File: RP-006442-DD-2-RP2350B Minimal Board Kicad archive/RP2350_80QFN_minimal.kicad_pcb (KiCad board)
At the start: 2 copper layers, 52 x 71.5 mm, 49 parts, among them J1 USB_B_Micro, J2 Conn_02x26_Odd_Even, J3 Conn_02x26_Odd_Even, J4 SM03B-SRSS-TB, SW1 SW_Push, SW2 SW_Push, U1 RP2350_80QFN, U2 NCP1117-3.3_SOT223, U3 W25Q128JVS, U4 DNF, Y1 ABM8-272-T3

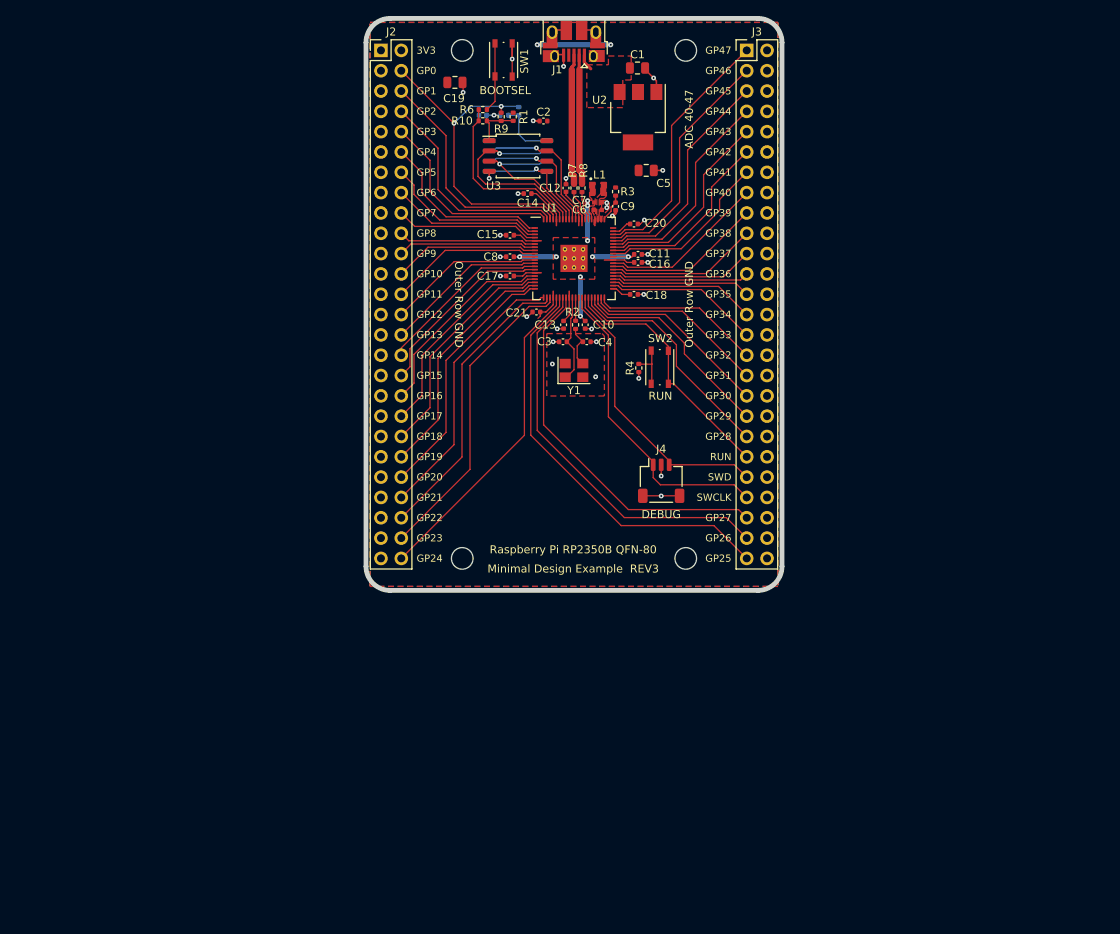
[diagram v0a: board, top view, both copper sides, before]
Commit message: Added debugprobe components to pcb
added pinheader connector to debug probe
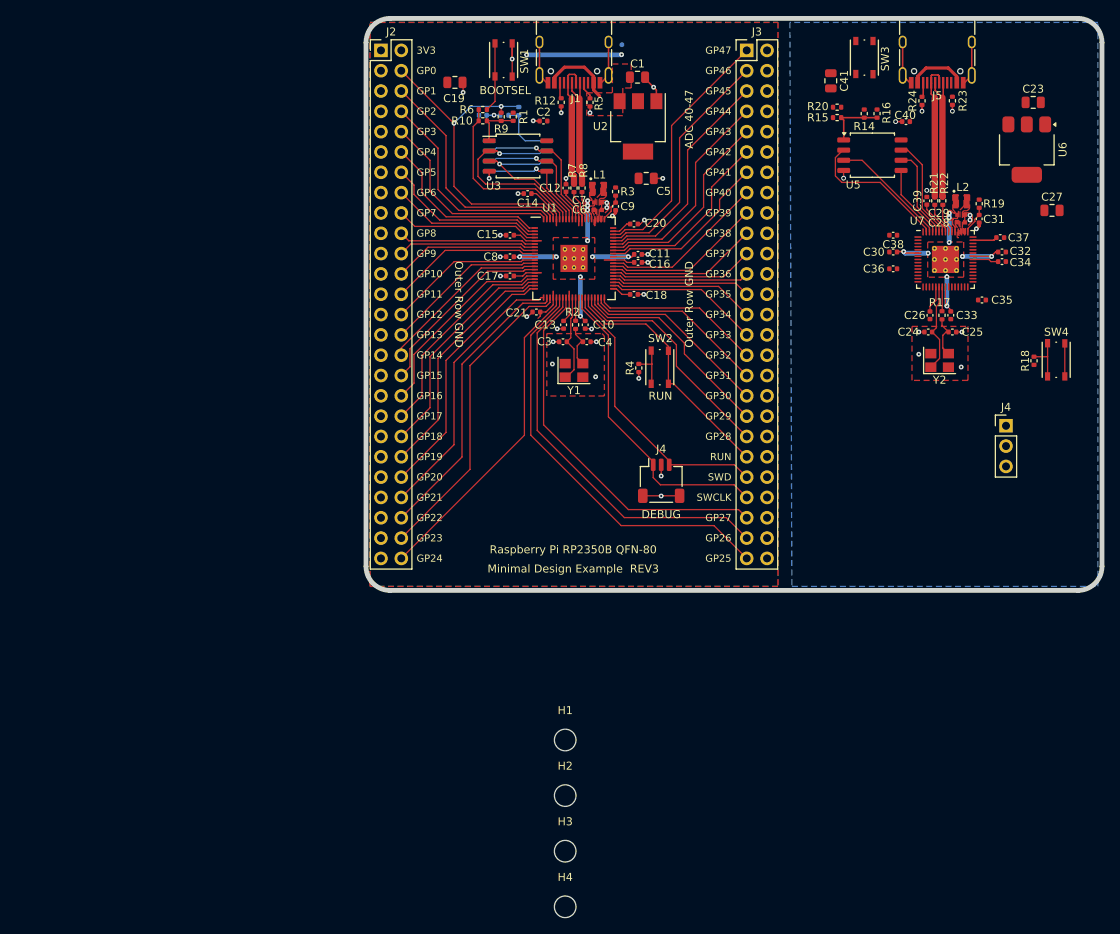
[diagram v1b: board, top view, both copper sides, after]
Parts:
- added C23: 10u, Capacitor_SMD:C_0805_2012Metric, F.Cu at (157.4, 80.5)
- added C24: 15p, Capacitor_SMD:C_0402_1005Metric, F.Cu at (144.3, 109.2)
- added C25: 15p, Capacitor_SMD:C_0402_1005Metric, F.Cu at (147.3, 109.2)
- added C26: 100n, Capacitor_SMD:C_0402_1005Metric, F.Cu at (144.5, 107.1)
- added C27: 10u, Capacitor_SMD:C_0805_2012Metric, F.Cu at (159.8, 94.0)
- added C28: 4.7u, RP2350_60QFN_minimal:C_0402_1005Metric_small_pads, F.Cu at (148.4, 95.5)
- added C29: 4.7u, RP2350_60QFN_minimal:C_0402_1005Metric_small_pads, F.Cu at (148.4, 94.5)
- added C30: 100n, Capacitor_SMD:C_0402_1005Metric, F.Cu at (139.9, 99.2)
- added C31: 4.7u, Capacitor_SMD:C_0402_1005Metric, F.Cu at (150.7, 95.0)
- added C32: 4.7u, Capacitor_SMD:C_0402_1005Metric, F.Cu at (153.5, 99.2)
- added C33: 100n, Capacitor_SMD:C_0402_1005Metric, F.Cu at (147.1, 107.1)
- added C34: 100n, Capacitor_SMD:C_0402_1005Metric, F.Cu at (153.5, 100.4)
- added C35: 100n, Capacitor_SMD:C_0402_1005Metric, F.Cu at (151.0, 105.2)
- added C36: 100n, Capacitor_SMD:C_0402_1005Metric, F.Cu at (139.9, 101.3)
- added C37: 100n, Capacitor_SMD:C_0402_1005Metric, F.Cu at (153.3, 97.4)
- added C38: 100n, Capacitor_SMD:C_0402_1005Metric, F.Cu at (139.9, 97.1)
- added C39: 100n, Capacitor_SMD:C_0402_1005Metric, F.Cu at (144.1, 92.8)
- added C40: 100n, Capacitor_SMD:C_0402_1005Metric, F.Cu at (141.5, 82.9)
- added C41: 10u, Capacitor_SMD:C_0805_2012Metric, F.Cu at (132.1, 77.8)
- added J4: Conn_01x03, Connector_PinHeader_2.54mm:PinHeader_1x03_P2.54mm_Vertical, F.Cu at (154.0, 120.9)
- added J5: USB_C_Receptacle_USB2.0_16P, Connector_USB:USB_C_Receptacle_HRO_TYPE-C-31-M-12, F.Cu at (145.4, 74.0)
- added L2: 3.3u, RP2350_60QFN_minimal:L_pol_2016, F.Cu at (148.4, 92.9)
- added R12: 5.1K, Resistor_SMD:R_0402_1005Metric, F.Cu at (98.4, 80.5)
- added R14: DNF, Resistor_SMD:R_0402_1005Metric, F.Cu at (136.3, 81.9)
- added R15: 0, Resistor_SMD:R_0402_1005Metric, F.Cu at (132.9, 82.4)
- added R16: DNF, Resistor_SMD:R_0402_1005Metric, F.Cu at (137.9, 81.9)
- added R17: 1k, Resistor_SMD:R_0402_1005Metric, F.Cu at (146.0, 107.1)
- added R18: 1k, Resistor_SMD:R_0402_1005Metric, F.Cu at (157.5, 112.8)
- added R19: 33, Resistor_SMD:R_0402_1005Metric, F.Cu at (150.7, 93.2)
- added R20: 1k, Resistor_SMD:R_0402_1005Metric, F.Cu at (132.9, 81.1)
- added R21: 27, Resistor_SMD:R_0402_1005Metric, F.Cu at (145.1, 92.8)
- added R22: 27, Resistor_SMD:R_0402_1005Metric, F.Cu at (146.1, 92.8)
- added R23: 5.1k, Resistor_SMD:R_0402_1005Metric, F.Cu at (147.3, 80.3)
- added R24: 5.1k, Resistor_SMD:R_0402_1005Metric, F.Cu at (143.5, 80.3)
- added R5: 5.1K, Resistor_SMD:R_0402_1005Metric, F.Cu at (102.0, 80.5)
- added SW3: SW_Push, Button_Switch_SMD:SW_Push_1P1T_NO_Vertical_Wuerth_434133025816, F.Cu at (136.3, 74.9)
- added SW4: SW_Push, Button_Switch_SMD:SW_Push_1P1T_NO_Vertical_Wuerth_434133025816, F.Cu at (160.3, 112.7)
- added U5: W25Q128JVS, Package_SO:SOIC-8_5.3x5.3mm_P1.27mm, F.Cu at (137.3, 87.1)
- added U6: NCP1117-3.3_SOT223, Package_TO_SOT_SMD:SOT-223-3_TabPin2, F.Cu at (156.6, 86.4)
- added U7: RP2350_60QFN, RP2350_60QFN_minimal:RP2350-QFN-60-1EP_7x7_P0.4mm_EP3.4x3.4mm_ThermalVias, F.Cu at (146.4, 100.1)
- added Y2: ABM8-272-T3, Crystal:Crystal_SMD_3225-4Pin_3.2x2.5mm, F.Cu at (145.7, 112.8)
- J1: value USB_B_Micro -> USB_C_Receptacle_USB2.0_16P; footprint Connector_USB:USB_Micro-B_Amphenol_10103594-0001LF_Horizontal -> Connector_USB:USB_C_Receptacle_HRO_TYPE-C-31-M-12
- moved H2 94.4 mm to (98.9, 167.2)
- moved H1 87.2 mm to (98.9, 160.2)
- moved H4 45.4 mm to (98.9, 181.1)
- moved H3 39.6 mm to (98.9, 174.1)
- moved J1 1.17 mm to (100.0, 74.0)
- moved U2 1.15 mm to (108.0, 83.5)
- moved C1 1.15 mm to (107.9, 77.3)
- moved C5 1.00 mm to (109.0, 90.0)
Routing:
- net +1V1: track 30.2 -> 55.5 mm, vias 9 -> 19
- net GND: track 38.8 -> 62.1 mm, vias 29 -> 42
- net /Debug probe/QSPI_SD1: track 0.00 -> 18.2 mm
- net +3V3: track 52.9 -> 70.6 mm
- net /Debug probe/USB_D+: track 0.00 -> 17.3 mm
- net /Debug probe/USB_D-: track 0.00 -> 16.5 mm
- net /Debug probe/QSPI_SD2: track 0.00 -> 14.7 mm
- net VBUS: track 2.11 -> 16.7 mm
- net /Debug probe/QSPI_SD3: track 0.00 -> 12.7 mm
- net /Debug probe/QSPI_SCLK: track 0.00 -> 11.5 mm
- net /Debug probe/XIN: track 0.00 -> 11.2 mm
- net /Debug probe/QSPI_SD0: track 0.00 -> 9.32 mm
- net /Debug probe/FLASH_SS: track 0.00 -> 7.41 mm
- net Net-(R18-Pad1): track 0.00 -> 5.85 mm
- net Net-(C25-Pad1): track 0.00 -> 5.39 mm
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- added copper zone on F.Cu, net /Debug probe/VREG_LX
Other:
- board size 52 x 71.5 mm -> 92 x 71.5 mm

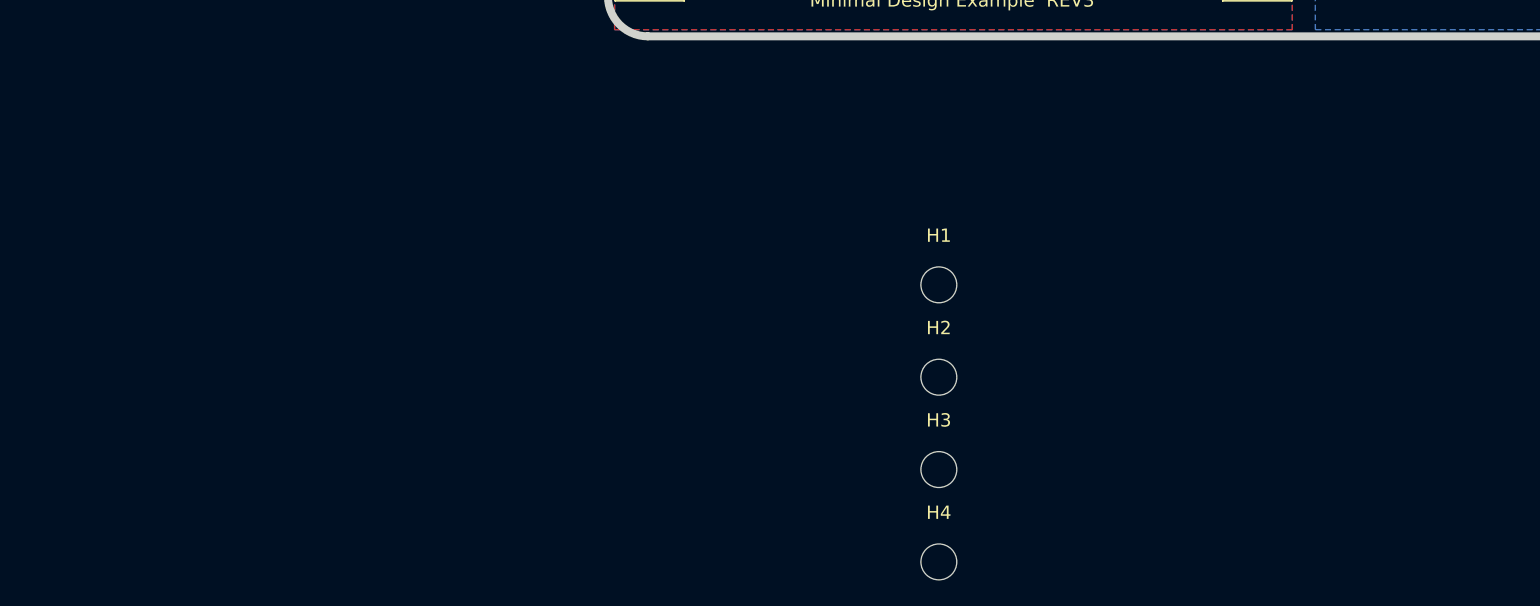
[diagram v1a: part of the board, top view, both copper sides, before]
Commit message: Created HT16K33-28SOP symbol
assigned new symbol footprint the pre-defined footprint for SOP-28 package
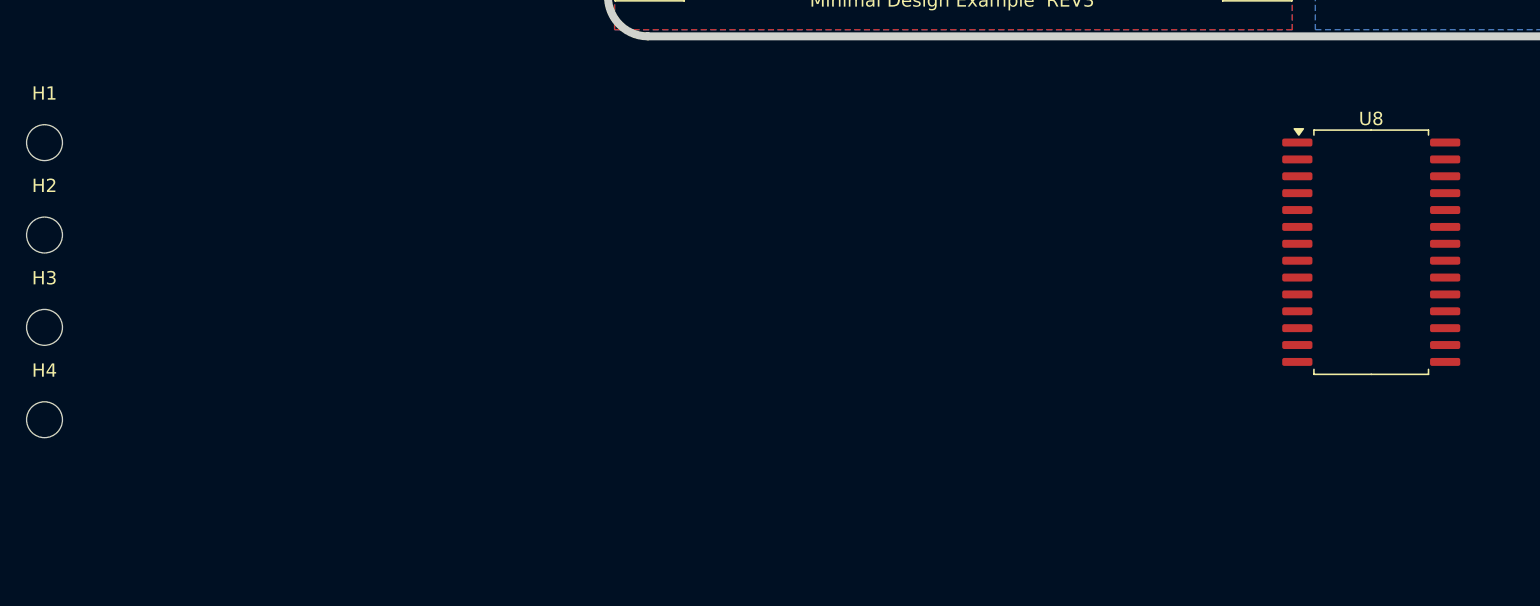
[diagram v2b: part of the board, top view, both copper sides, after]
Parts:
- added U8: HT16K33A-28SOP, Package_SO:SOP-28_8.4x18.16mm_P1.27mm, F.Cu at (131.4, 157.7)
- moved H2 68.1 mm to (31.6, 156.4)
- moved H4 68.1 mm to (31.6, 170.3)
- moved H1 68.1 mm to (31.6, 149.5)
- moved H3 68.1 mm to (31.6, 163.4)

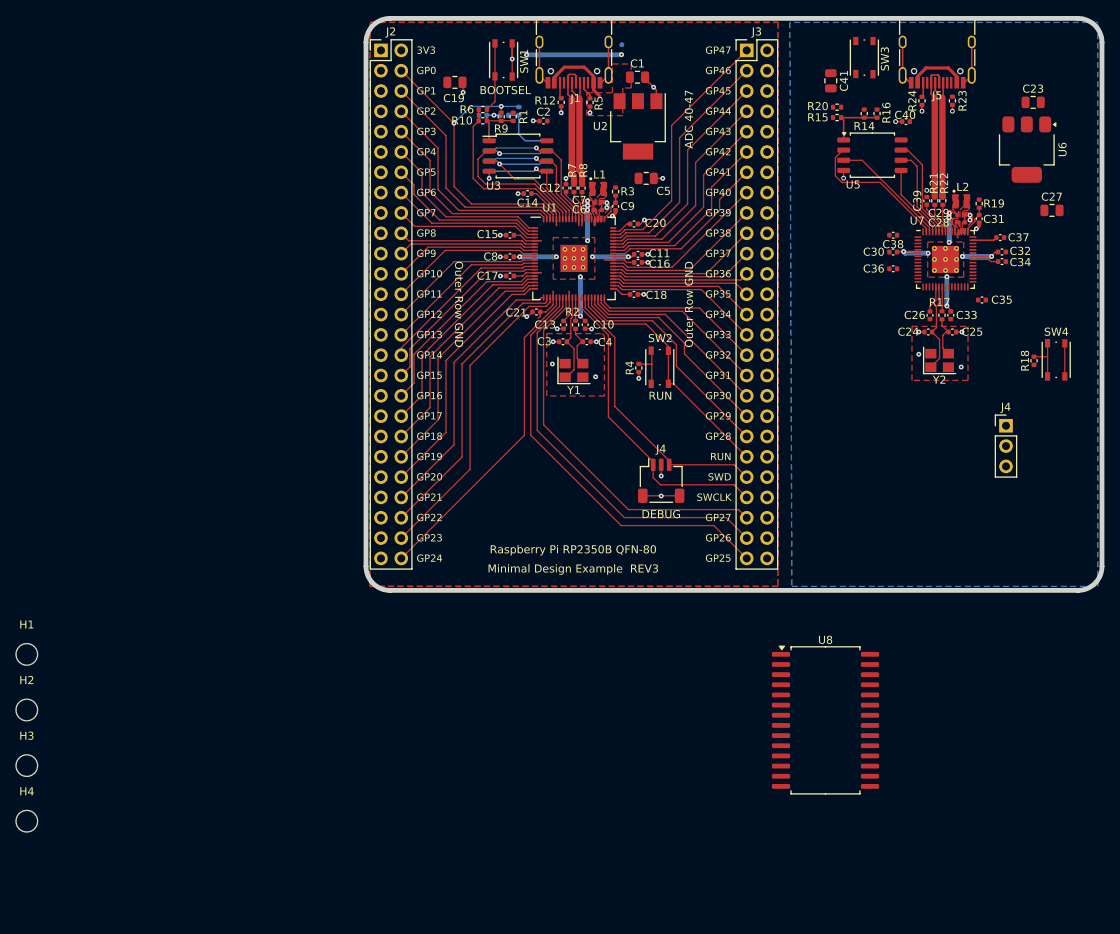
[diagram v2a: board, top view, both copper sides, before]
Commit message: Update hex displays
Added 7-segment display symbol, labels, i2c pull-up resistors, capacitor.

Synced added components to pcb.
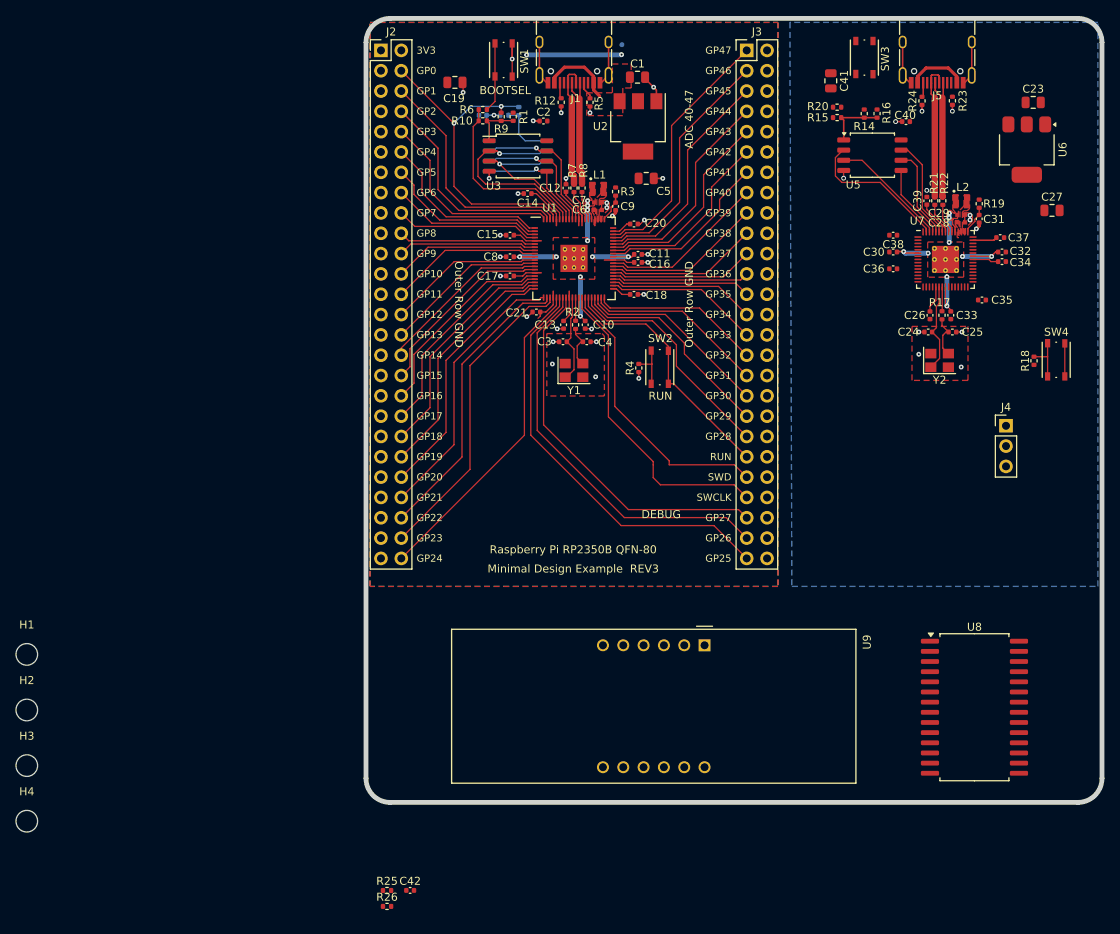
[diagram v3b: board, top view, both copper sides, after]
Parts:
- removed the J4 at (110.9, 127.8)
- added C42: 100n, Capacitor_SMD:C_0402_1005Metric, F.Cu at (79.5, 179.0)
- added R25: 4.7k, Resistor_SMD:R_0402_1005Metric, F.Cu at (76.6, 179.0)
- added R26: 4.7k, Resistor_SMD:R_0402_1005Metric, F.Cu at (76.6, 181.0)
- added U9: CC56-12EWA, Display_7Segment:CA56-12EWA, F.Cu at (116.3, 148.4)
- moved U8 18.7 mm to (150.1, 156.1)
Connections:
- U8 pad 1: unconnected-(U8-VSS-Pad1) -> GND
- U8 pad 18: unconnected-(U8-ROW7/K5-Pad18) -> /Hex displays peripheral/ROW7
- U8 pad 19: unconnected-(U8-ROW6/K4-Pad19) -> /Hex displays peripheral/ROW6
- U8 pad 2: unconnected-(U8-COM0/AD-Pad2) -> /Hex displays peripheral/COM0
- U8 pad 20: unconnected-(U8-ROW5/K3-Pad20) -> /Hex displays peripheral/ROW5
- U8 pad 21: unconnected-(U8-ROW4/K2-Pad21) -> /Hex displays peripheral/ROW4
- U8 pad 22: unconnected-(U8-ROW3/K1-Pad22) -> /Hex displays peripheral/ROW3
- U8 pad 23: unconnected-(U8-ROW2/A0-Pad23) -> /Hex displays peripheral/ROW2
- U8 pad 24: unconnected-(U8-ROW1/A1-Pad24) -> /Hex displays peripheral/ROW1
- U8 pad 25: unconnected-(U8-ROW0/A2-Pad25) -> /Hex displays peripheral/ROW0
- U8 pad 26: unconnected-(U8-SCL-Pad26) -> /Hex displays peripheral/SCL
- U8 pad 27: unconnected-(U8-SDA-Pad27) -> /Hex displays peripheral/SDA
- U8 pad 28: unconnected-(U8-VDD-Pad28) -> /Hex displays peripheral/VDD
- U8 pad 3: unconnected-(U8-COM1/KS0-Pad3) -> /Hex displays peripheral/COM1
- U8 pad 4: unconnected-(U8-COM2/KS1-Pad4) -> /Hex displays peripheral/COM2
- U8 pad 5: unconnected-(U8-COM3/KS2-Pad5) -> /Hex displays peripheral/COM3
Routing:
- net GND: track 62.1 -> 56.0 mm, vias 42 -> 40
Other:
- board size 92 x 71.5 mm -> 92 x 98 mm

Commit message: Update RP2350_80QFN_minimal.kicad_pcb
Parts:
- moved SW4 3.77 mm to (157.6, 110.0), turned to 180 degrees
- moved C23 2.40 mm to (155.0, 80.5)
- moved U6 2.40 mm to (154.2, 86.4)
- moved C1 1.40 mm to (107.9, 78.8)
- moved U2 1.15 mm to (108.0, 84.7)
- moved C5 1.00 mm to (109.0, 91.0)
- moved R18 0.25 mm to (157.8, 112.8), turned to 0 degrees

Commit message: Updated pcb
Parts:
- moved J4 3.25 mm to (155.0, 124.0), turned to -90 degrees
- moved C27 3.04 mm to (156.8, 93.5)
- moved C41 1.30 mm to (130.8, 77.8)
- moved C38 1.14 mm to (141.0, 96.8)
- moved C30 0.51 mm to (139.8, 99.7)
- moved C36 0.14 mm to (139.8, 101.4)
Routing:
- net /Debug probe/GPIO0: track 0.00 -> 30.4 mm, vias 0 -> 2
- net /Debug probe/QSPI_SS: track 0.00 -> 23.2 mm
- net /SWCLK: track 38.9 -> 61.3 mm, vias 0 -> 2
- net /SWD: track 35.6 -> 48.5 mm, vias 0 -> 2
- net /Debug probe/RUN: track 4.12 -> 14.9 mm
- net GND: track 56.1 -> 65.8 mm, vias 40 -> 47
- net /Debug probe/~{USB_BOOT}: track 0.00 -> 9.71 mm
- net /Debug probe/SWD: track 0.00 -> 8.62 mm
- net +3V3: track 70.6 -> 79.0 mm
